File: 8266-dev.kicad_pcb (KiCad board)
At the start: 2 copper layers, 99.1 x 97.8 mm, 31 parts, among them J1 Programming headers, J2 Left breakout, J3 Bottom breakout, J4 Right breakout, J5 USB_B_Micro, Q1 BSS138, U1 ESP8266-12F_ESP-12F, U2 CH330N

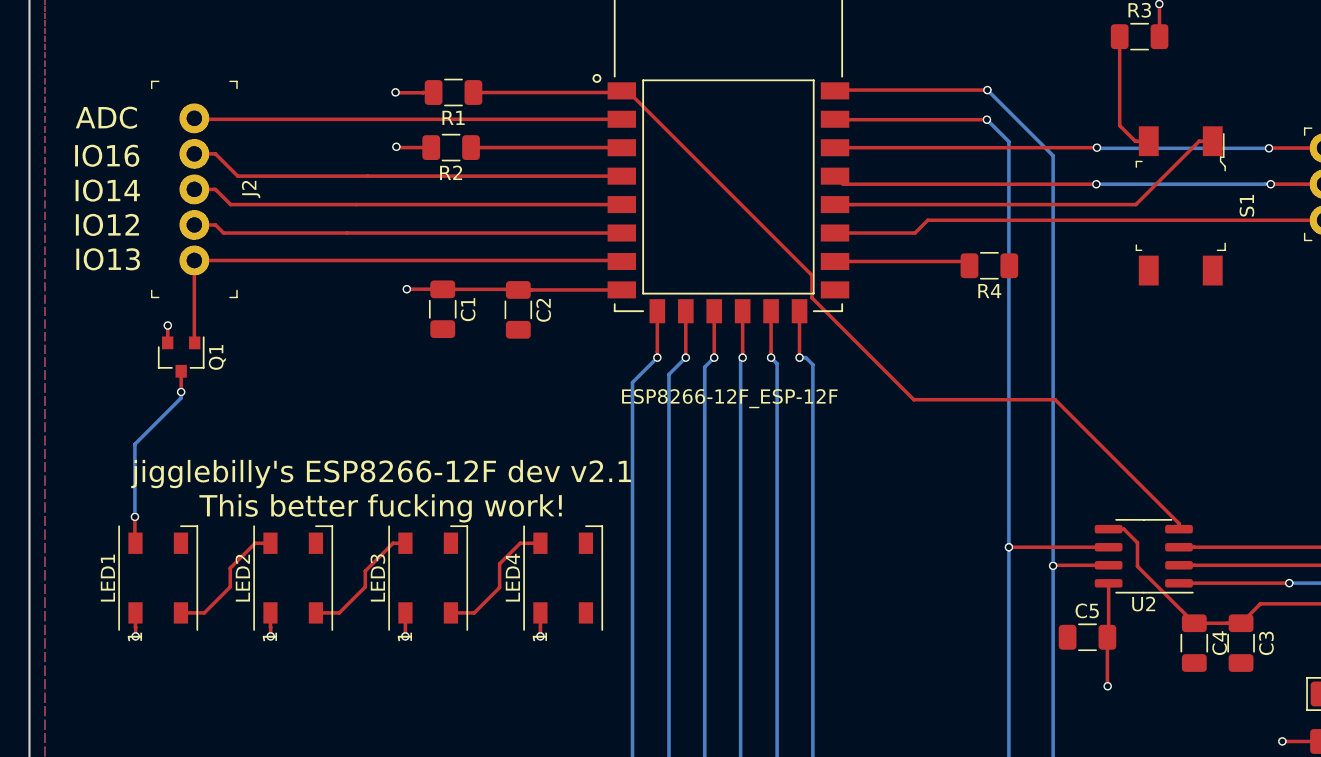
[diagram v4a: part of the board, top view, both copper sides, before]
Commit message: added LDO and re-swapped the tx/rx lines, removed one cap
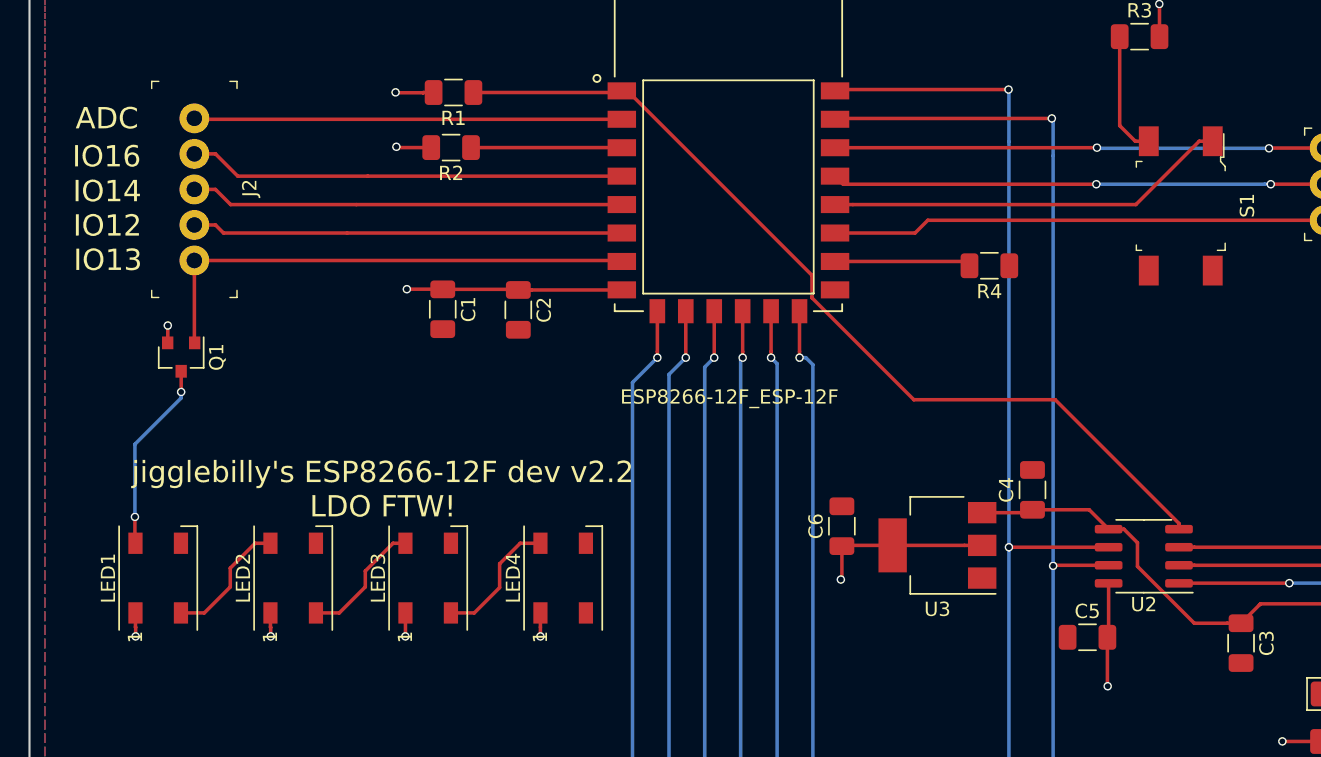
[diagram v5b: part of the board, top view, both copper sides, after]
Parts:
- removed the G*** at (0.00, 0.00) (x6)
- added C6: 1uF, Capacitor_SMD:C_1206_3216Metric, F.Cu at (141.0, 85.8)
- added G*** (x6): LOGO, LOGO, F.Cu at (0.00, 0.00)
- added U3: TLV1117-33, Package_TO_SOT_SMD:SOT-223-3_TabPin2, F.Cu at (147.7, 87.1)
- C4: value 100nF -> 1uF
- moved C4 15.7 mm to (154.4, 83.2), turned to 90 degrees
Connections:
- C5 pad 2: /VCC -> Net-(C5-Pad2)
- U1 pad 21: /tx -> /rx
- U1 pad 22: /rx -> /tx
- U2 pad 8: /VCC -> Net-(C5-Pad2)
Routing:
- net /VBUS: track 23.3 -> 32.8 mm
- net Net-(C5-Pad2): track 0.00 -> 7.28 mm, vias 0 -> 1
- net /VCC: track 46.0 -> 51.0 mm
- net /tx: track 96.5 -> 99.5 mm
- net /rx: track 96.6 -> 97.2 mm
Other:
- board text added: "jigglebilly's ESP8266-12F dev v2.2 LDO FTW!"
- board text removed: "jigglebilly's ESP8266-12F dev v2.1 This better fucking work!"

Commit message: latest version
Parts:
- removed the G*** at (0.00, 0.00) (x6)
- added G*** (x6): LOGO, LOGO, F.Cu at (0.00, 0.00)
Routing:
- net Net-(C5-Pad2): track 7.28 -> 3.83 mm, vias 1 -> 0
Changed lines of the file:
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@@
     (thickness 1.6)
     (drawings 24)
-    (tracks 256)
+    (tracks 253)
     (zones 0)
     (modules 33)
@@
       (drillshape 0)
       (scaleselection 1)
-      (outputdirectory "gerbers-v2.1-power-light/"))
+      (outputdirectory "gerbers-v2.2-LDO-FTW/"))
   )
   (net 0 "")
@@
   (segment (start 159.7309 93.5228) (end 159.64454 93.60916) (width 0.25) (layer F.Cu) (net 36))
   (segment (start 159.7309 89.8144) (end 159.7309 93.5228) (width 0.25) (layer F.Cu) (net 36))
-  (via (at 159.6644 97.05086) (size 0.6) (drill 0.4) (layers F.Cu B.Cu) (net 36))
-  (segment (start 159.64454 93.60916) (end 159.64454 97.031) (width 0.25) (layer F.Cu) (net 36))
-  (segment (start 159.64454 97.031) (end 159.6644 97.05086) (width 0.25) (layer F.Cu) (net 36))
   (segment (start 165.7559 87.2744) (end 164.6809 87.2744) (width 0.25) (layer F.Cu) (net 2))
   (segment (start 176.743802 87.2744) (end 165.7559 87.2744) (width 0.25) (layer F.Cu) (net 2))
